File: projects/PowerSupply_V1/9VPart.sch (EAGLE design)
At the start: 24 parts, among them IC1 LM2596T, IC2 LM2596T, X1 IN, X2 OUT

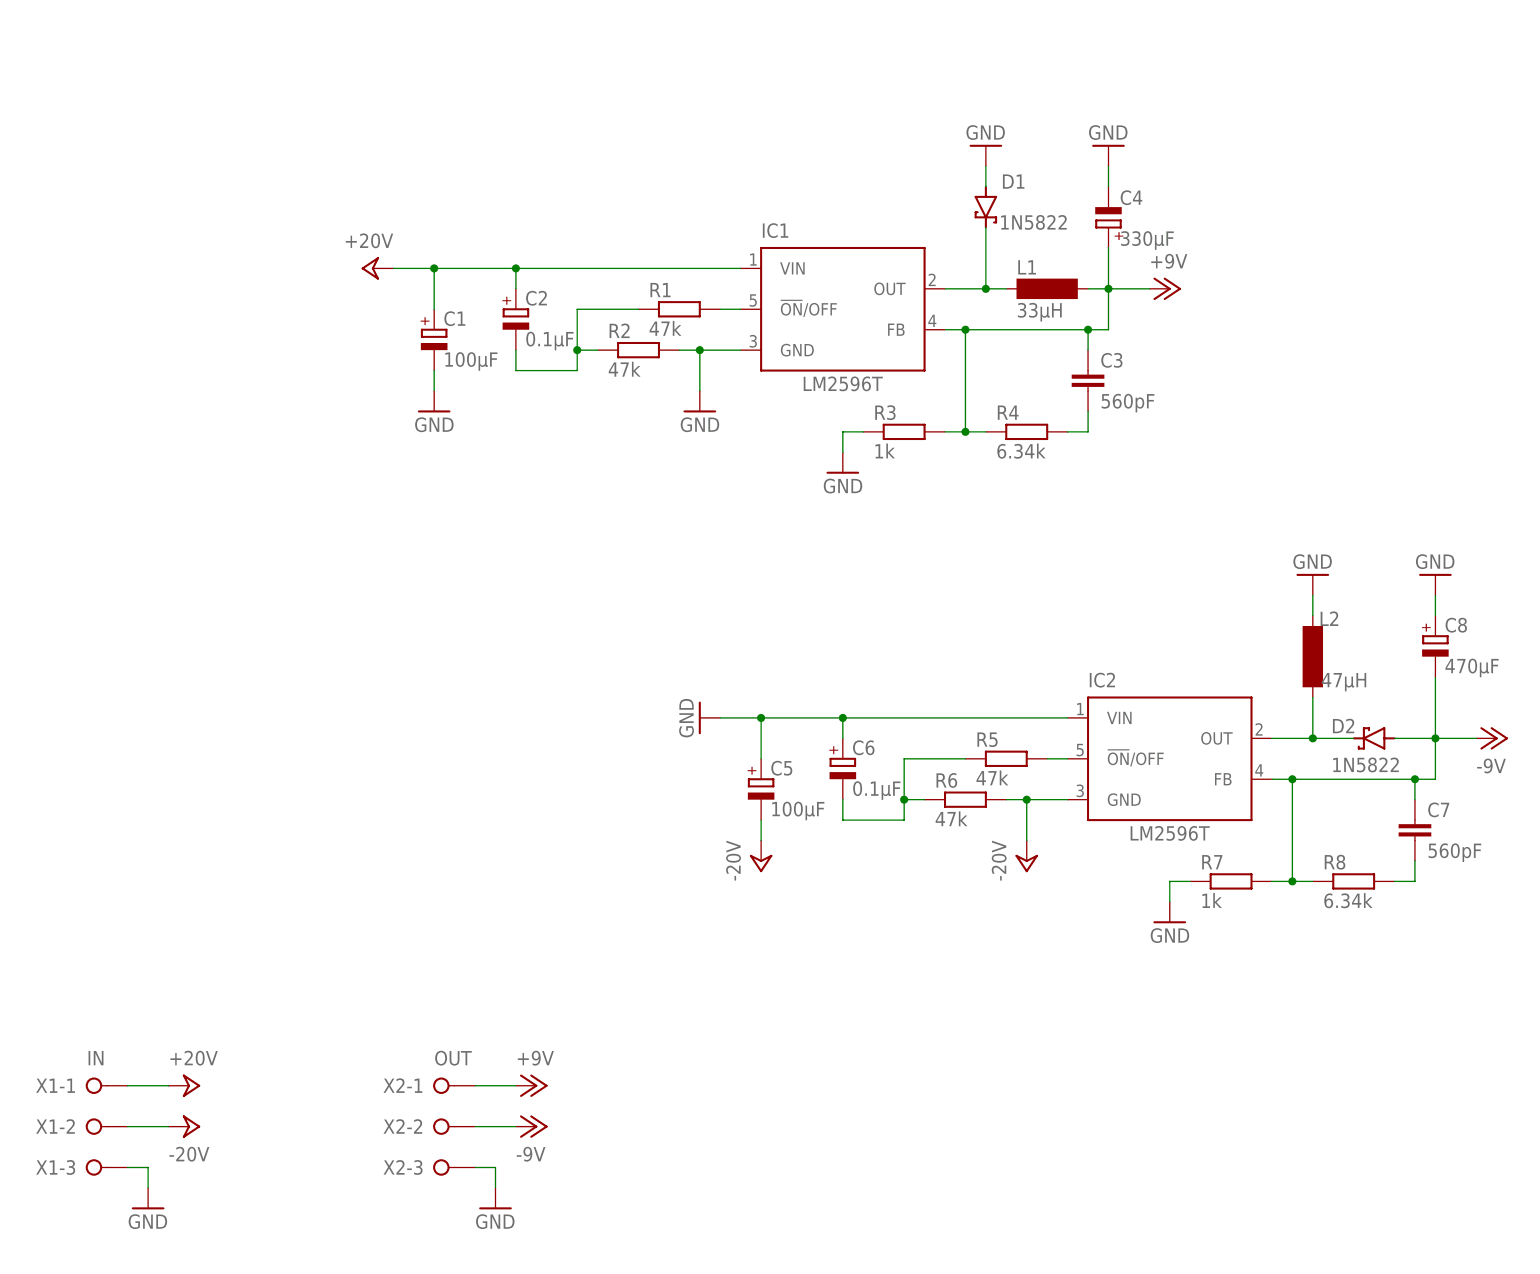
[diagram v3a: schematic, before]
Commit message: refactor(all): schematics and routing changed
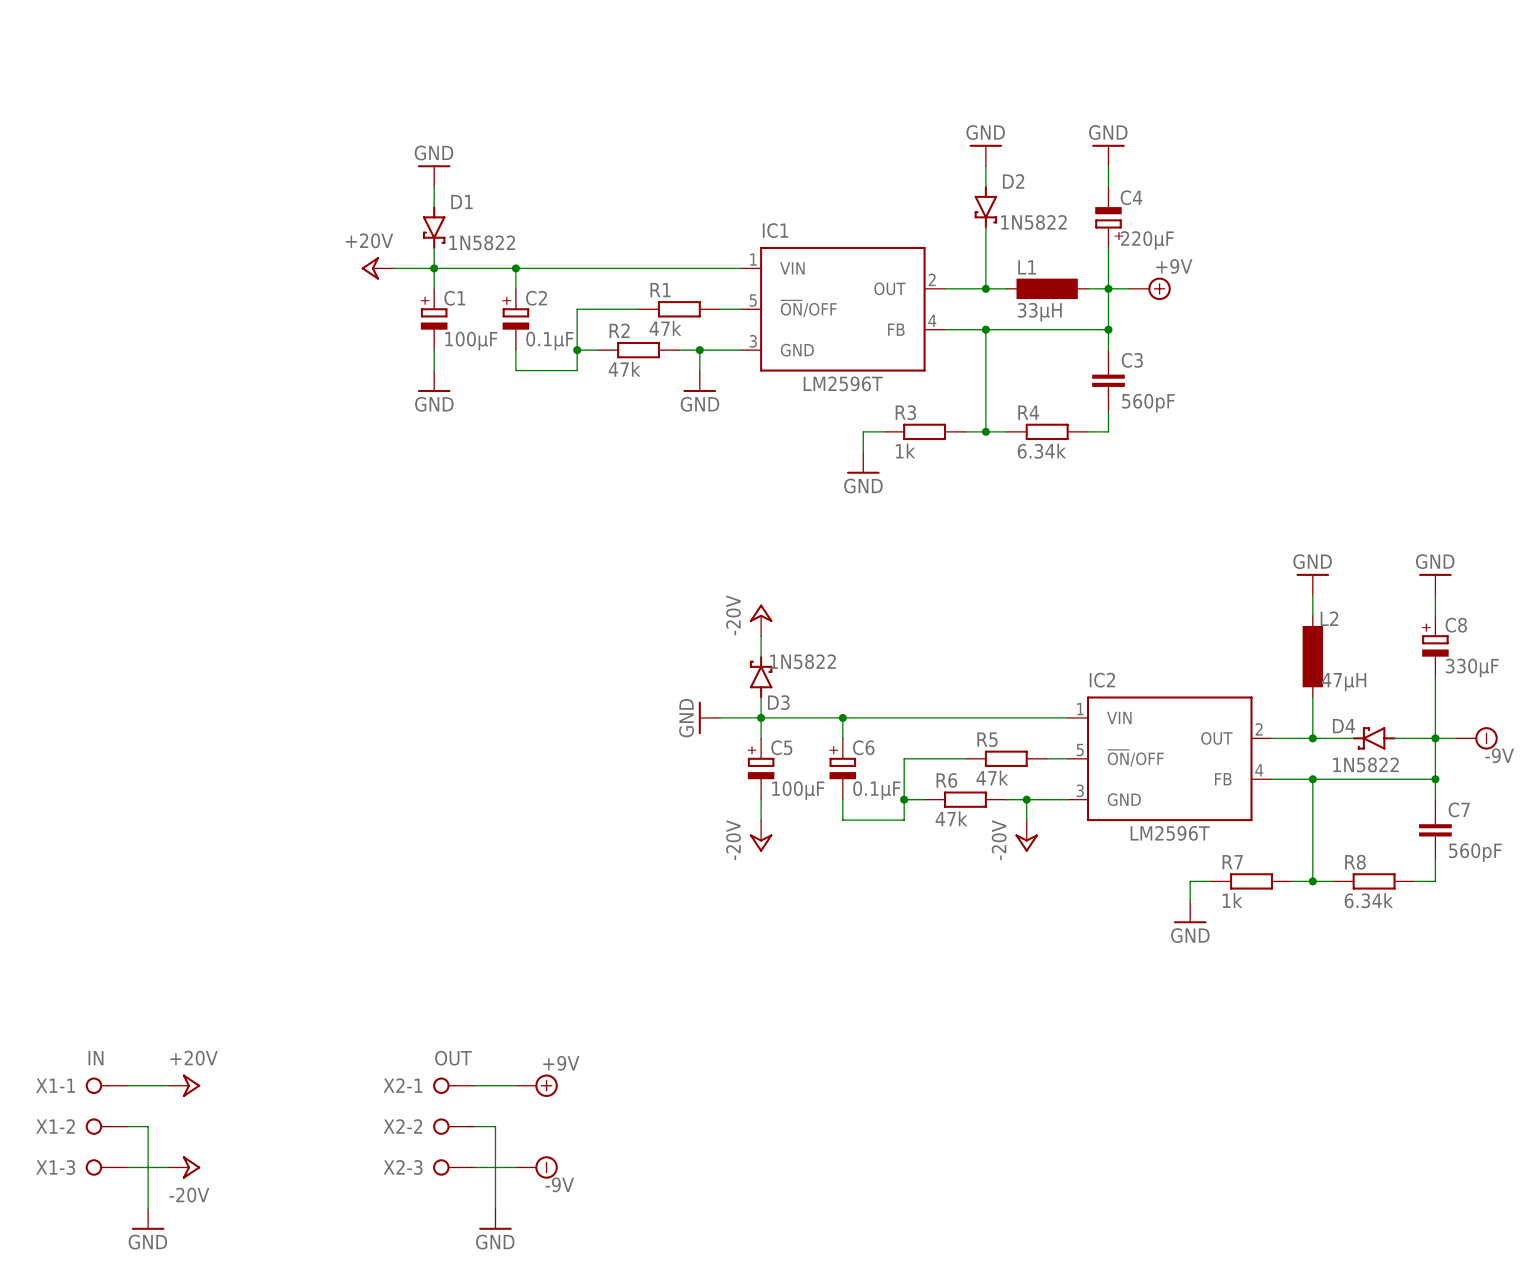
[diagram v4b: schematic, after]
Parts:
- added D3, D4: 1N5822, diode:SCHOTTKY-DIODEC4111-15
- C4: value 330µF -> 220µF
- C8: value 470µF -> 330µF
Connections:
- net +12V renamed +9V
- removed net -12V: C7.1, C8.-, D2.A, IC2.FB, R7.2, R8.1, X2-2.KL
- new net -9V: C7.1, C8.-, D4.A, IC2.FB, R7.2, R8.1, X2-3.KL
- net +24V: now also D1.C
- net -24V: now also D3.C, X1-3.KL; no longer X1-2.KL
- net GND: now also D2.A, D3.A, X1-2.KL, X2-2.KL; no longer X1-3.KL, X2-3.KL
- net N$2: now also D4.C; no longer D2.C
- net N$3: now also D2.C; no longer D1.C
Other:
- moved on the sheet: C1, C3, C5, C7, D1, D2, R3, R4, R7, R8

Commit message: feat: 9VPart refactored
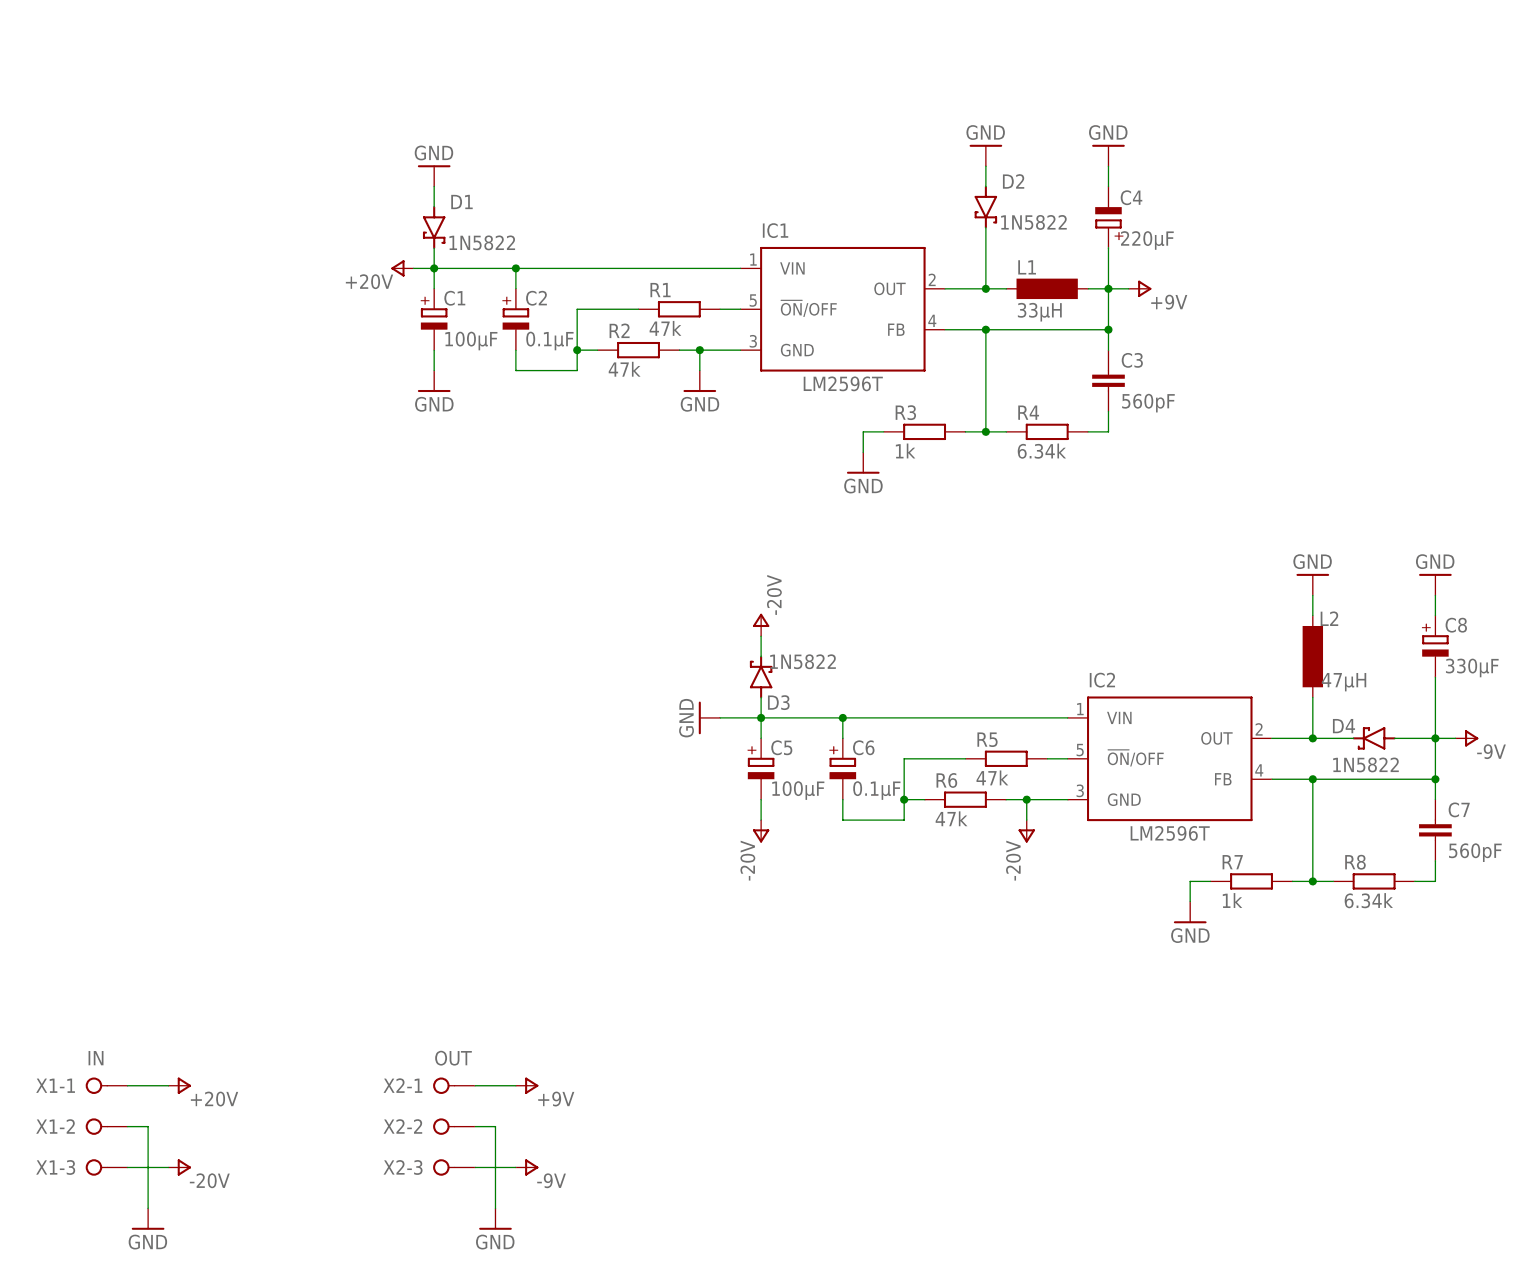
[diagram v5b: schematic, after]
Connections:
- net +24V renamed +20V
- net -24V renamed -20V
